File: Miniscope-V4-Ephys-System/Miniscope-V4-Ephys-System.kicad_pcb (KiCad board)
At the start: 4 copper layers, 24.2 x 15.5 mm, 67 parts, among them J1 34 Circuit Slimslack Connector, J10 Conn_01x01, J11 Conn_01x01, J12 Conn_01x01, J13 Conn_01x01, J14 Conn_01x05, J15 Conn_01x01, J16 Conn_01x01, J17 Conn_01x01, J18 Conn_01x01, J19 Conn_01x01, J2 Conn_01x01, J20 Conn_01x01, J21 Conn_01x01, J22 Conn_01x01, J23 Conn_01x01, J24 Conn_01x01, J25 Conn_01x01, J26 Conn_01x01, J27 Conn_01x01, J28 Conn_01x01, J3 Conn_01x01, J4 Conn_01x01, J5 Conn_01x01, J6 Conn_01x01, J7 Conn_01x01, J8 Conn_01x01, J9 Conn_01x01, Q1 MMBT3904LP-7B, U1 RHD2132, U2 TXB0304RUT, U3 MCP1711T-30I/5X, U4 ATSAME70N21A-CN, U5 MCP1711T-18I/5X, Y1 SMD_CRYSTAL

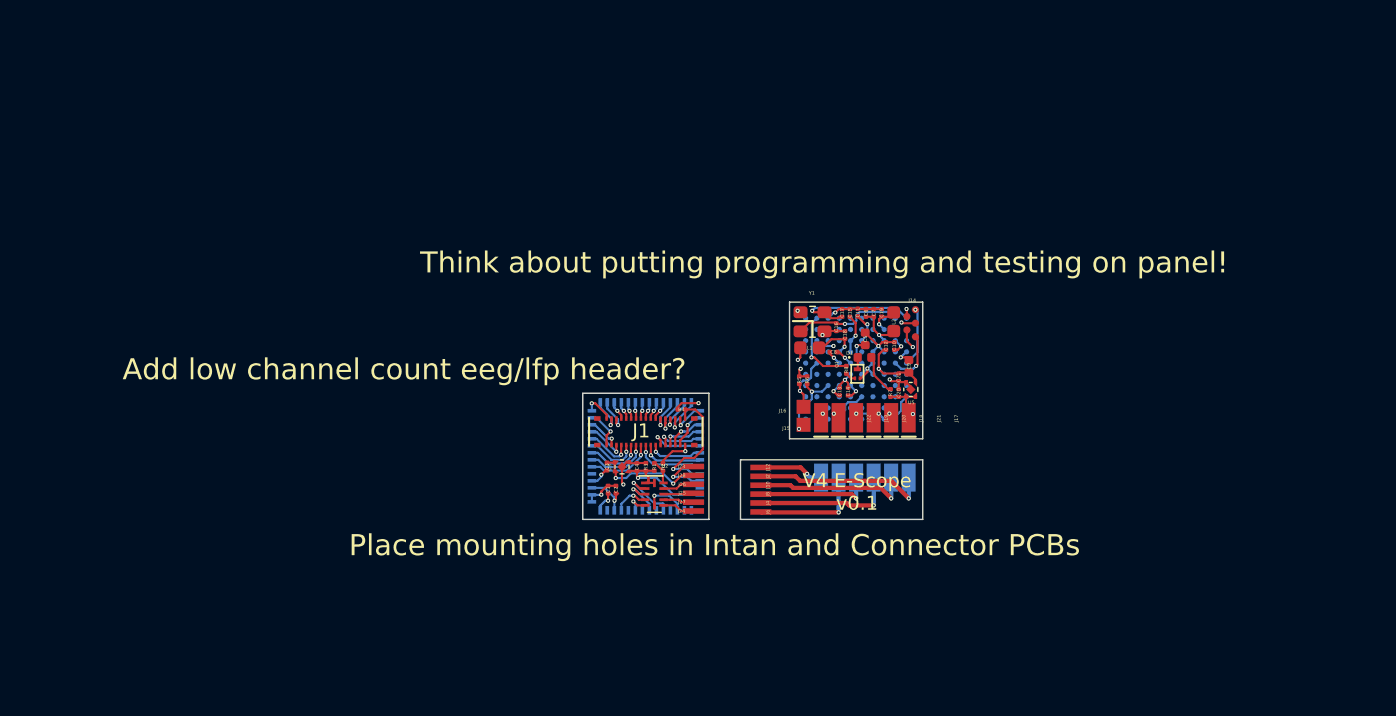
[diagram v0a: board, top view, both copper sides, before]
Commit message: Add mouse bites and panel the 3 PCBs.
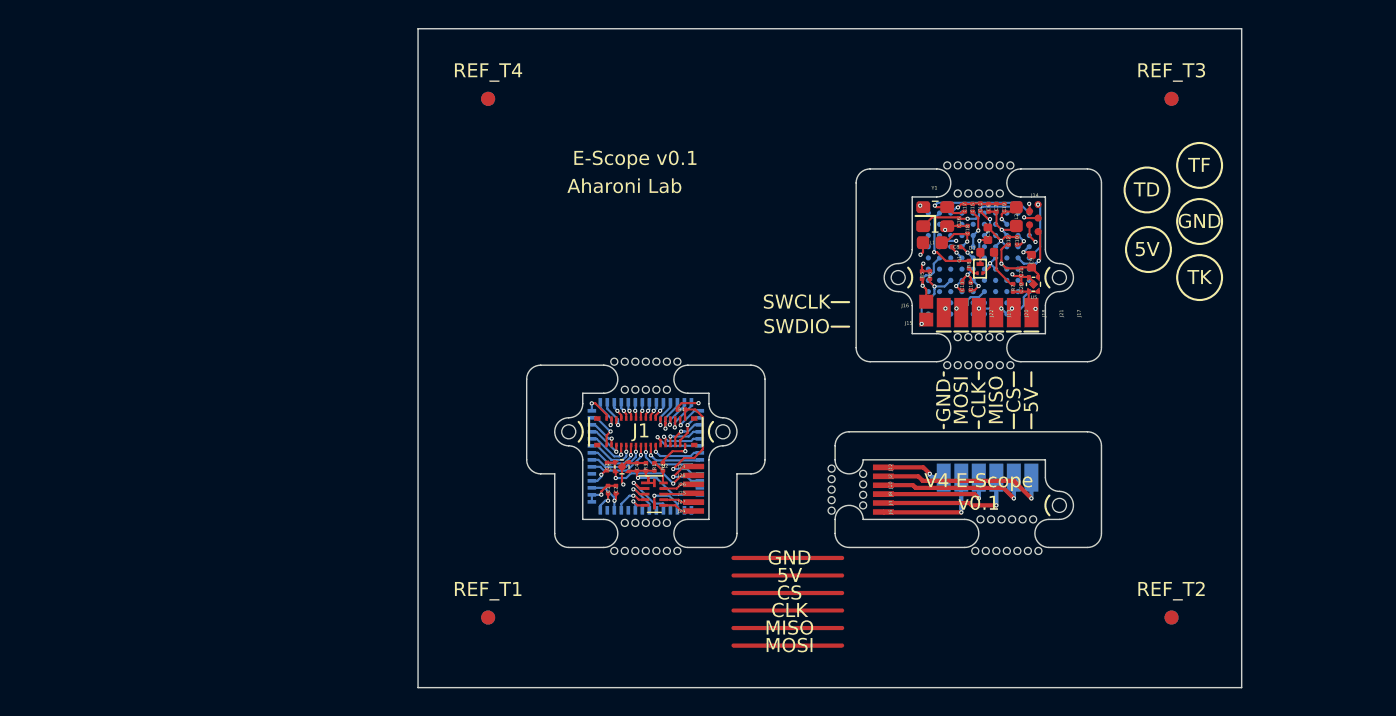
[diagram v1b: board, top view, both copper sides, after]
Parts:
- added HOLE: Conn_1x1_700_Circular_Pad, .Connector:Conn_1x1_700_Circular_Pad, F.Cu at (138.9, 135.0)
- added HOLE: Conn_1x1_700_Circular_Pad, .Connector:Conn_1x1_700_Circular_Pad, F.Cu at (137.0, 137.2)
- added HOLE: Conn_1x1_700_Circular_Pad, .Connector:Conn_1x1_700_Circular_Pad, F.Cu at (136.6, 135.0)
- added HOLE: Conn_1x1_700_Circular_Pad, .Connector:Conn_1x1_700_Circular_Pad, F.Cu at (135.9, 135.0)
- added HOLE: Conn_1x1_700_Circular_Pad, .Connector:Conn_1x1_700_Circular_Pad, F.Cu at (135.5, 137.2)
- added HOLE: Conn_1x1_700_Circular_Pad, .Connector:Conn_1x1_700_Circular_Pad, F.Cu at (124.5, 131.4)
- added HOLE: Conn_1x1_700_Circular_Pad, .Connector:Conn_1x1_700_Circular_Pad, F.Cu at (124.5, 134.4)
- added HOLE: Conn_1x1_700_Circular_Pad, .Connector:Conn_1x1_700_Circular_Pad, F.Cu at (126.8, 131.8)
- added HOLE: Conn_1x1_700_Circular_Pad, .Connector:Conn_1x1_700_Circular_Pad, F.Cu at (113.5, 137.2)
- added HOLE: Conn_1x1_700_Circular_Pad, .Connector:Conn_1x1_700_Circular_Pad, F.Cu at (109.0, 137.2)
- added HOLE: Conn_1x1_700_Circular_Pad, .Connector:Conn_1x1_700_Circular_Pad, F.Cu at (109.0, 123.8)
- added HOLE: Conn_1x1_700_Circular_Pad, .Connector:Conn_1x1_700_Circular_Pad, F.Cu at (139.2, 137.2)
- added HOLE: Conn_1x1_700_Circular_Pad, .Connector:Conn_1x1_700_Circular_Pad, F.Cu at (113.5, 123.8)
- added HOLE: Conn_1x1_700_Circular_Pad, .Connector:Conn_1x1_700_Circular_Pad, F.Cu at (132.8, 109.8)
- added HOLE: Conn_1x1_700_Circular_Pad, .Connector:Conn_1x1_700_Circular_Pad, F.Cu at (137.2, 109.8)
- added HOLE: Conn_1x1_700_Circular_Pad, .Connector:Conn_1x1_700_Circular_Pad, F.Cu at (137.2, 124.0)
- added HOLE: Conn_1x1_700_Circular_Pad, .Connector:Conn_1x1_700_Circular_Pad, F.Cu at (132.8, 124.0)
- added HOLE: Conn_1x1_700_Circular_Pad, .Connector:Conn_1x1_700_Circular_Pad, F.Cu at (124.5, 132.9)
- added HOLE: Conn_1x1_700_Circular_Pad, .Connector:Conn_1x1_700_Circular_Pad, F.Cu at (126.8, 132.5)
- added HOLE: Conn_1x1_700_Circular_Pad, .Connector:Conn_1x1_700_Circular_Pad, F.Cu at (124.5, 133.6)
- added HOLE: Conn_1x1_700_Circular_Pad, .Connector:Conn_1x1_700_Circular_Pad, F.Cu at (126.8, 134.0)
- added HOLE: Conn_1x1_700_Circular_Pad, .Connector:Conn_1x1_700_Circular_Pad, F.Cu at (126.8, 133.2)
- added HOLE: Conn_1x1_700_Circular_Pad, .Connector:Conn_1x1_700_Circular_Pad, F.Cu at (134.8, 137.2)
- added HOLE: Conn_1x1_700_Circular_Pad, .Connector:Conn_1x1_700_Circular_Pad, F.Cu at (124.5, 132.1)
- added HOLE: Conn_1x1_700_Circular_Pad, .Connector:Conn_1x1_700_Circular_Pad, F.Cu at (135.8, 122.0)
- added HOLE: Conn_1x1_700_Circular_Pad, .Connector:Conn_1x1_700_Circular_Pad, F.Cu at (134.2, 124.0)
- added HOLE: Conn_1x1_700_Circular_Pad, .Connector:Conn_1x1_700_Circular_Pad, F.Cu at (133.5, 122.0)
- added HOLE: Conn_1x1_700_Circular_Pad, .Connector:Conn_1x1_700_Circular_Pad, F.Cu at (136.5, 122.0)
- added HOLE: Conn_1x1_700_Circular_Pad, .Connector:Conn_1x1_700_Circular_Pad, F.Cu at (135.8, 124.0)
- added HOLE: Conn_1x1_700_Circular_Pad, .Connector:Conn_1x1_700_Circular_Pad, F.Cu at (136.5, 124.0)
- added HOLE: Conn_1x1_700_Circular_Pad, .Connector:Conn_1x1_700_Circular_Pad, F.Cu at (135.0, 124.0)
- added HOLE: Conn_1x1_700_Circular_Pad, .Connector:Conn_1x1_700_Circular_Pad, F.Cu at (135.0, 122.0)
- added HOLE: Conn_1x1_700_Circular_Pad, .Connector:Conn_1x1_700_Circular_Pad, F.Cu at (134.2, 122.0)
- added HOLE: Conn_1x1_700_Circular_Pad, .Connector:Conn_1x1_700_Circular_Pad, F.Cu at (137.4, 135.0)
- added HOLE: Conn_1x1_700_Circular_Pad, .Connector:Conn_1x1_700_Circular_Pad, F.Cu at (133.5, 124.0)
- added HOLE: Conn_1x1_700_Circular_Pad, .Connector:Conn_1x1_700_Circular_Pad, F.Cu at (134.2, 111.8)
- added HOLE: Conn_1x1_700_Circular_Pad, .Connector:Conn_1x1_700_Circular_Pad, F.Cu at (135.8, 109.8)
- added HOLE: Conn_1x1_700_Circular_Pad, .Connector:Conn_1x1_700_Circular_Pad, F.Cu at (136.5, 111.8)
- added HOLE: Conn_1x1_700_Circular_Pad, .Connector:Conn_1x1_700_Circular_Pad, F.Cu at (133.5, 111.8)
- added HOLE: Conn_1x1_700_Circular_Pad, .Connector:Conn_1x1_700_Circular_Pad, F.Cu at (134.2, 109.8)
- added HOLE: Conn_1x1_700_Circular_Pad, .Connector:Conn_1x1_700_Circular_Pad, F.Cu at (133.5, 109.8)
- added HOLE: Conn_1x1_700_Circular_Pad, .Connector:Conn_1x1_700_Circular_Pad, F.Cu at (135.0, 109.8)
- added HOLE: Conn_1x1_700_Circular_Pad, .Connector:Conn_1x1_700_Circular_Pad, F.Cu at (135.0, 111.8)
- added HOLE: Conn_1x1_700_Circular_Pad, .Connector:Conn_1x1_700_Circular_Pad, F.Cu at (135.8, 111.8)
- added HOLE: Conn_1x1_700_Circular_Pad, .Connector:Conn_1x1_700_Circular_Pad, F.Cu at (136.2, 137.2)
- added HOLE: Conn_1x1_700_Circular_Pad, .Connector:Conn_1x1_700_Circular_Pad, F.Cu at (136.5, 109.8)
- added HOLE: Conn_1x1_700_Circular_Pad, .Connector:Conn_1x1_700_Circular_Pad, F.Cu at (110.5, 123.8)
- added HOLE: Conn_1x1_700_Circular_Pad, .Connector:Conn_1x1_700_Circular_Pad, F.Cu at (109.8, 123.8)
- added HOLE: Conn_1x1_700_Circular_Pad, .Connector:Conn_1x1_700_Circular_Pad, F.Cu at (112.0, 123.8)
- added HOLE: Conn_1x1_700_Circular_Pad, .Connector:Conn_1x1_700_Circular_Pad, F.Cu at (112.8, 123.8)
- added HOLE: Conn_1x1_700_Circular_Pad, .Connector:Conn_1x1_700_Circular_Pad, F.Cu at (111.2, 123.8)
- added HOLE: Conn_1x1_700_Circular_Pad, .Connector:Conn_1x1_700_Circular_Pad, F.Cu at (110.5, 125.8)
- added HOLE: Conn_1x1_700_Circular_Pad, .Connector:Conn_1x1_700_Circular_Pad, F.Cu at (109.8, 125.8)
- added HOLE: Conn_1x1_700_Circular_Pad, .Connector:Conn_1x1_700_Circular_Pad, F.Cu at (112.0, 125.8)
- added HOLE: Conn_1x1_700_Circular_Pad, .Connector:Conn_1x1_700_Circular_Pad, F.Cu at (112.8, 125.8)
- added HOLE: Conn_1x1_700_Circular_Pad, .Connector:Conn_1x1_700_Circular_Pad, F.Cu at (135.1, 135.0)
- added HOLE: Conn_1x1_700_Circular_Pad, .Connector:Conn_1x1_700_Circular_Pad, F.Cu at (111.2, 125.8)
- added HOLE: Conn_1x1_700_Circular_Pad, .Connector:Conn_1x1_700_Circular_Pad, F.Cu at (110.5, 137.2)
- added HOLE: Conn_1x1_700_Circular_Pad, .Connector:Conn_1x1_700_Circular_Pad, F.Cu at (109.8, 137.2)
- added HOLE: Conn_1x1_700_Circular_Pad, .Connector:Conn_1x1_700_Circular_Pad, F.Cu at (112.0, 137.2)
- added HOLE: Conn_1x1_700_Circular_Pad, .Connector:Conn_1x1_700_Circular_Pad, F.Cu at (112.8, 137.2)
- added HOLE: Conn_1x1_700_Circular_Pad, .Connector:Conn_1x1_700_Circular_Pad, F.Cu at (111.2, 137.2)
- added HOLE: Conn_1x1_700_Circular_Pad, .Connector:Conn_1x1_700_Circular_Pad, F.Cu at (112.8, 135.2)
- added HOLE: Conn_1x1_700_Circular_Pad, .Connector:Conn_1x1_700_Circular_Pad, F.Cu at (112.0, 135.2)
- added HOLE: Conn_1x1_700_Circular_Pad, .Connector:Conn_1x1_700_Circular_Pad, F.Cu at (111.2, 135.2)
- added HOLE: Conn_1x1_700_Circular_Pad, .Connector:Conn_1x1_700_Circular_Pad, F.Cu at (110.5, 135.2)
- added HOLE: Conn_1x1_700_Circular_Pad, .Connector:Conn_1x1_700_Circular_Pad, F.Cu at (138.1, 135.0)
- added HOLE: Conn_1x1_700_Circular_Pad, .Connector:Conn_1x1_700_Circular_Pad, F.Cu at (109.8, 135.2)
- added HOLE: Conn_1x1_700_Circular_Pad, .Connector:Conn_1x1_700_Circular_Pad, F.Cu at (140.8, 134.0)
- added HOLE: Conn_1x1_700_Circular_Pad, .Connector:Conn_1x1_700_Circular_Pad, F.Cu at (105.8, 128.8)
- added HOLE: Conn_1x1_700_Circular_Pad, .Connector:Conn_1x1_700_Circular_Pad, F.Cu at (116.8, 128.8)
- added HOLE: Conn_1x1_700_Circular_Pad, .Connector:Conn_1x1_700_Circular_Pad, F.Cu at (140.8, 117.8)
- added HOLE: Conn_1x1_700_Circular_Pad, .Connector:Conn_1x1_700_Circular_Pad, F.Cu at (129.2, 117.8)
- added HOLE: Conn_1x1_700_Circular_Pad, .Connector:Conn_1x1_700_Circular_Pad, F.Cu at (137.8, 137.2)
- added HOLE: Conn_1x1_700_Circular_Pad, .Connector:Conn_1x1_700_Circular_Pad, F.Cu at (138.5, 137.2)
- added REF_B1: Fiducial_1mm_Mask2mm, Fiducial:Fiducial_1mm_Mask2mm, B.Cu at (100.0, 142.0)
- added REF_B2: Fiducial_1mm_Mask2mm, Fiducial:Fiducial_1mm_Mask2mm, B.Cu at (148.8, 142.0)
- added REF_B3: Fiducial_1mm_Mask2mm, Fiducial:Fiducial_1mm_Mask2mm, B.Cu at (148.8, 105.0)
- added REF_B4: Fiducial_1mm_Mask2mm, Fiducial:Fiducial_1mm_Mask2mm, B.Cu at (100.0, 105.0)
- added REF_T1: Fiducial_1mm_Mask2mm, Fiducial:Fiducial_1mm_Mask2mm, F.Cu at (100.0, 142.0)
- added REF_T2: Fiducial_1mm_Mask2mm, Fiducial:Fiducial_1mm_Mask2mm, F.Cu at (148.8, 142.0)
- added REF_T3: Fiducial_1mm_Mask2mm, Fiducial:Fiducial_1mm_Mask2mm, F.Cu at (148.8, 105.0)
- added REF_T4: Fiducial_1mm_Mask2mm, Fiducial:Fiducial_1mm_Mask2mm, F.Cu at (100.0, 105.0)
- moved C11 11.5 mm to (135.1, 112.7)
- moved C13 11.5 mm to (133.8, 118.4)
- moved C14 11.5 mm to (134.4, 118.4)
- moved C16 11.5 mm to (133.6, 113.8)
- moved C18 11.5 mm to (134.2, 114.3)
- moved C5 11.5 mm to (135.6, 114.6)
- moved C7 11.5 mm to (136.3, 112.8)
- moved C10 11.5 mm to (137.7, 115.1)
- moved C12 11.5 mm to (137.1, 115.1)
- moved C17 11.5 mm to (134.0, 112.8)
- moved C19 11.5 mm to (136.8, 112.8)
- moved C20 11.5 mm to (138.0, 118.5)
- moved C21 11.5 mm to (138.0, 117.4)
- moved C8 11.5 mm to (133.4, 115.6)
- moved C9 11.5 mm to (138.8, 116.6)
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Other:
- board size 24.2 x 15.5 mm -> 58.8 x 47 mm
- board text added: "5V"
- board text added: "Aharoni Lab"
- board text added: "CLK"
- board text added: "CS"
- board text added: "E-Scope v0.1"
- board text added: "GND"
- board text added: "MISO"
- board text added: "MOSI"
- board text added: "SWCLK"
- board text added: "SWDIO"
- board text added: "TD"
- board text added: "TF"
- board text added: "TK"
- board text removed: "Add low channel count eeg/lfp header?"
- board text removed: "Place mounting holes in Intan and Connector PCBs"
- board text removed: "Think about putting programming and testing on panel!"

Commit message: Add files via upload
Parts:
- added HOLE: Conn_1x1_700_Circular_Pad, .Connector:Conn_1x1_700_Circular_Pad, F.Cu at (107.8, 119.9)
- added HOLE: Conn_1x1_700_Circular_Pad, .Connector:Conn_1x1_700_Circular_Pad, F.Cu at (110.8, 111.0)
- added HOLE: Conn_1x1_700_Circular_Pad, .Connector:Conn_1x1_700_Circular_Pad, F.Cu at (110.0, 113.0)
- added HOLE: Conn_1x1_700_Circular_Pad, .Connector:Conn_1x1_700_Circular_Pad, F.Cu at (109.3, 113.0)
- added HOLE: Conn_1x1_700_Circular_Pad, .Connector:Conn_1x1_700_Circular_Pad, F.Cu at (109.3, 111.0)
- added HOLE: Conn_1x1_700_Circular_Pad, .Connector:Conn_1x1_700_Circular_Pad, F.Cu at (107.8, 111.0)
- added HOLE: Conn_1x1_700_Circular_Pad, .Connector:Conn_1x1_700_Circular_Pad, F.Cu at (108.5, 111.0)
- added HOLE: Conn_1x1_700_Circular_Pad, .Connector:Conn_1x1_700_Circular_Pad, F.Cu at (107.8, 113.0)
- added HOLE: Conn_1x1_700_Circular_Pad, .Connector:Conn_1x1_700_Circular_Pad, F.Cu at (110.8, 113.0)
- added HOLE: Conn_1x1_700_Circular_Pad, .Connector:Conn_1x1_700_Circular_Pad, F.Cu at (110.0, 111.0)
- added HOLE: Conn_1x1_700_Circular_Pad, .Connector:Conn_1x1_700_Circular_Pad, F.Cu at (108.5, 113.0)
- added HOLE: Conn_1x1_700_Circular_Pad, .Connector:Conn_1x1_700_Circular_Pad, F.Cu at (108.5, 121.9)
- added HOLE: Conn_1x1_700_Circular_Pad, .Connector:Conn_1x1_700_Circular_Pad, F.Cu at (107.8, 121.9)
- added HOLE: Conn_1x1_700_Circular_Pad, .Connector:Conn_1x1_700_Circular_Pad, F.Cu at (108.5, 119.9)
- added HOLE: Conn_1x1_700_Circular_Pad, .Connector:Conn_1x1_700_Circular_Pad, F.Cu at (109.3, 119.9)
- added HOLE: Conn_1x1_700_Circular_Pad, .Connector:Conn_1x1_700_Circular_Pad, F.Cu at (109.3, 121.9)
- added HOLE: Conn_1x1_700_Circular_Pad, .Connector:Conn_1x1_700_Circular_Pad, F.Cu at (110.8, 121.9)
- added HOLE: Conn_1x1_700_Circular_Pad, .Connector:Conn_1x1_700_Circular_Pad, F.Cu at (110.0, 121.9)
- added HOLE: Conn_1x1_700_Circular_Pad, .Connector:Conn_1x1_700_Circular_Pad, F.Cu at (110.8, 119.9)
- added HOLE: Conn_1x1_700_Circular_Pad, .Connector:Conn_1x1_700_Circular_Pad, F.Cu at (110.0, 119.9)
- added HOLE: Conn_1x1_700_Circular_Pad, .Connector:Conn_1x1_700_Circular_Pad, F.Cu at (107.0, 121.9)
- added HOLE: Conn_1x1_700_Circular_Pad, .Connector:Conn_1x1_700_Circular_Pad, F.Cu at (111.5, 121.9)
- added HOLE: Conn_1x1_700_Circular_Pad, .Connector:Conn_1x1_700_Circular_Pad, F.Cu at (111.5, 111.0)
- added HOLE: Conn_1x1_700_Circular_Pad, .Connector:Conn_1x1_700_Circular_Pad, F.Cu at (107.0, 111.0)
- added HOLE: Conn_1x1_700_Circular_Pad, .Connector:Conn_1x1_700_Circular_Pad, F.Cu at (103.5, 115.6)
- added HOLE: Conn_1x1_700_Circular_Pad, .Connector:Conn_1x1_700_Circular_Pad, F.Cu at (115.0, 115.6)
- added J10: Conn_01x01, .Connector:Conn_1x1_250x750_Pad, F.Cu at (105.7, 117.2)
- added J12: Conn_01x01, .Connector:Conn_1x1_250x750_Pad, F.Cu at (105.7, 115.9)
- added J13: Conn_01x01, .Connector:Conn_1x1_250x750_Pad, B.Cu at (113.3, 118.4)
- added J2: Conn_01x01, .Connector:Conn_1x1_250x750_Pad, F.Cu at (105.7, 116.6)
- added J3: Conn_01x01, .Connector:Conn_1x1_250x750_Pad, B.Cu at (105.4, 118.9)
- added J3: Conn_01x01, .Connector:Conn_1x1_250x750_Pad, B.Cu at (105.4, 117.6)
- added J3: Conn_01x01, .Connector:Conn_1x1_250x750_Pad, B.Cu at (107.1, 118.4)
- added J4: Conn_01x01, .Connector:Conn_1x1_250x750_Pad, F.Cu at (105.7, 118.5)
- added J6: Conn_01x01, .Connector:Conn_1x1_250x750_Pad, F.Cu at (105.7, 119.1)
- added J8: Conn_01x01, .Connector:Conn_1x1_250x750_Pad, F.Cu at (105.7, 117.8)
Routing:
- net (no net): track 0.00 -> 28.6 mm, vias 0 -> 2
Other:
- outline, holes or cut-outs redrawn

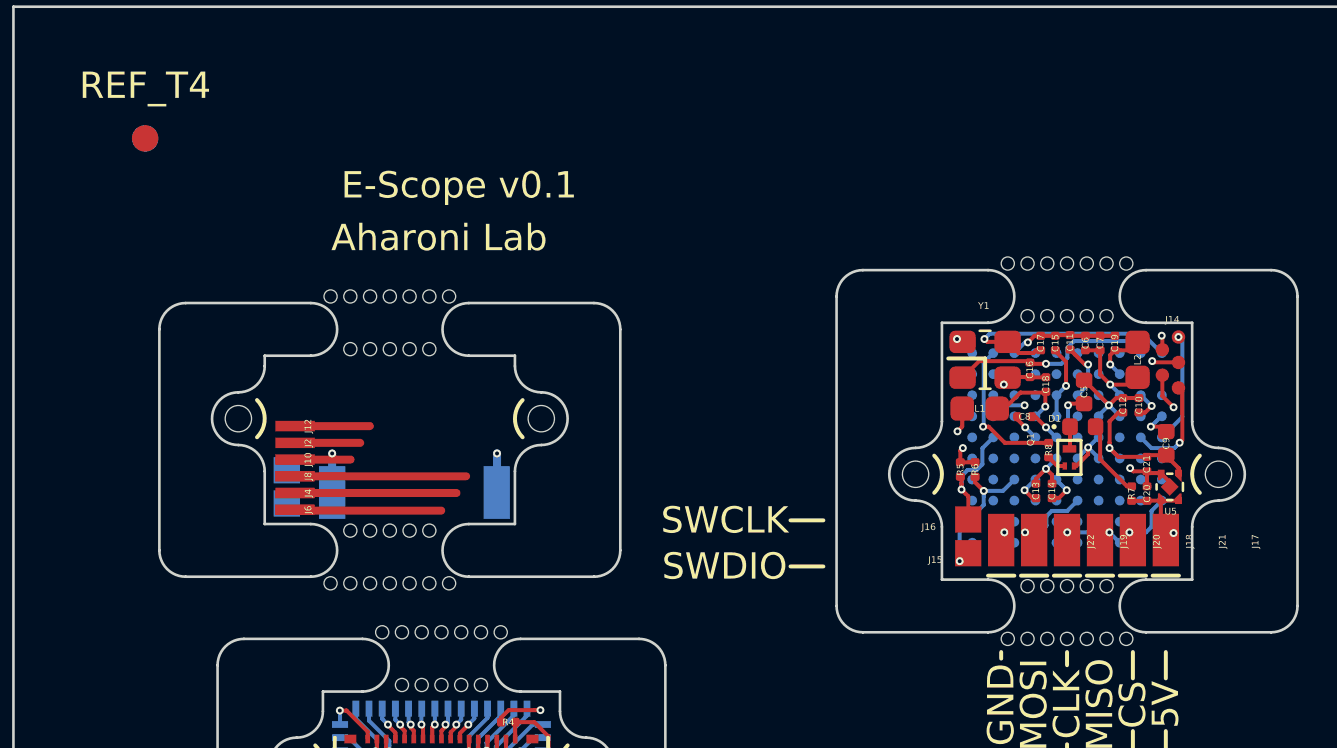
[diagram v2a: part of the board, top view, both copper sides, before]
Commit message: Revert "updated ephys pcb with low profile connectors and started programming board"
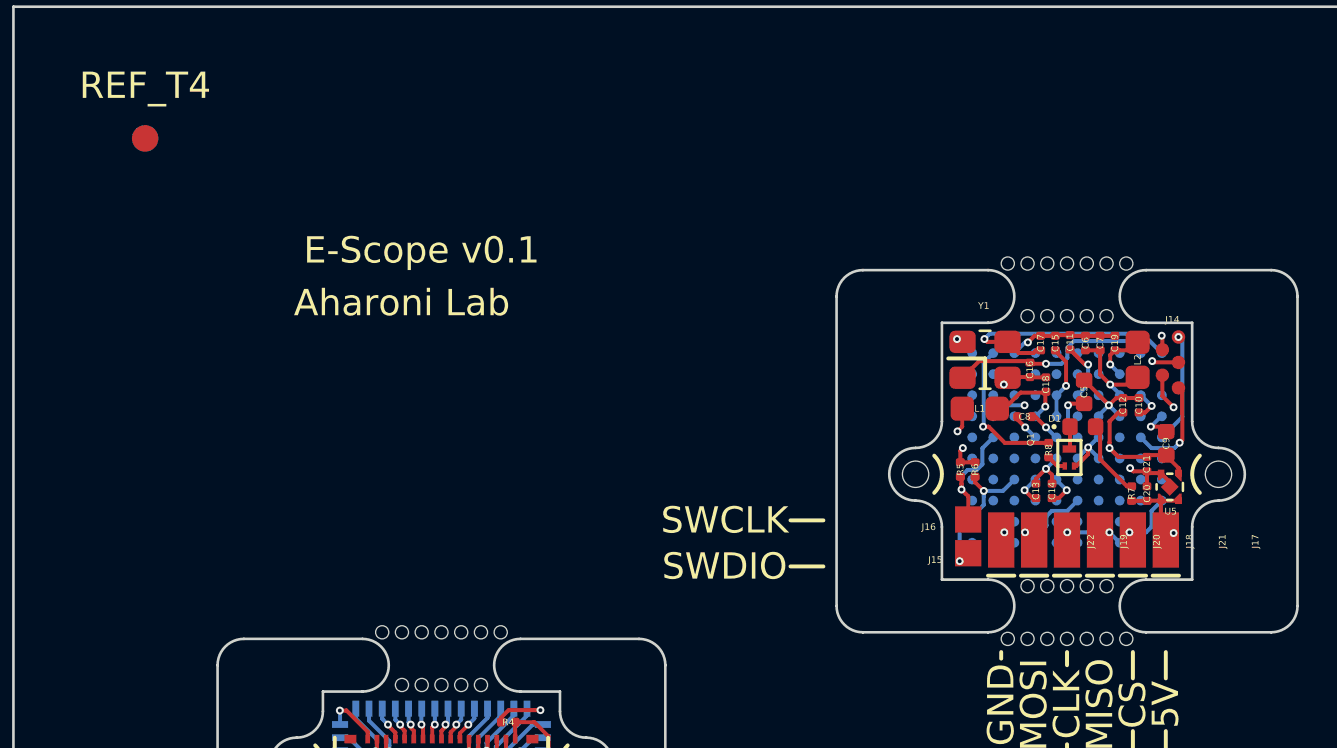
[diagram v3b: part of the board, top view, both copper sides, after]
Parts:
- removed the HOLE at (107.8, 119.9)
- removed the HOLE at (110.8, 111.0)
- removed the HOLE at (110.0, 113.0)
- removed the HOLE at (109.3, 113.0)
- removed the HOLE at (109.3, 111.0)
- removed the HOLE at (107.8, 111.0)
- removed the HOLE at (108.5, 111.0)
- removed the HOLE at (107.8, 113.0)
- removed the HOLE at (110.8, 113.0)
- removed the HOLE at (110.0, 111.0)
- removed the HOLE at (108.5, 113.0)
- removed the HOLE at (108.5, 121.9)
- removed the HOLE at (107.8, 121.9)
- removed the HOLE at (108.5, 119.9)
- removed the HOLE at (109.3, 119.9)
- removed the HOLE at (109.3, 121.9)
- removed the HOLE at (110.8, 121.9)
- removed the HOLE at (110.0, 121.9)
- removed the HOLE at (110.8, 119.9)
- removed the HOLE at (110.0, 119.9)
- removed the HOLE at (107.0, 121.9)
- removed the HOLE at (111.5, 121.9)
- removed the HOLE at (111.5, 111.0)
- removed the HOLE at (107.0, 111.0)
- removed the HOLE at (103.5, 115.6)
- removed the HOLE at (115.0, 115.6)
- removed the J10 at (105.7, 117.2)
- removed the J12 at (105.7, 115.9)
- removed the J13 at (113.3, 118.4)
- removed the J2 at (105.7, 116.6)
- removed the J3 at (105.4, 118.9)
- removed the J3 at (105.4, 117.6)
- removed the J3 at (107.1, 118.4)
- removed the J4 at (105.7, 118.5)
- removed the J6 at (105.7, 119.1)
- removed the J8 at (105.7, 117.8)
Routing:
- net (no net): track 28.6 -> 0.00 mm, vias 2 -> 0
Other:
- outline, holes or cut-outs redrawn

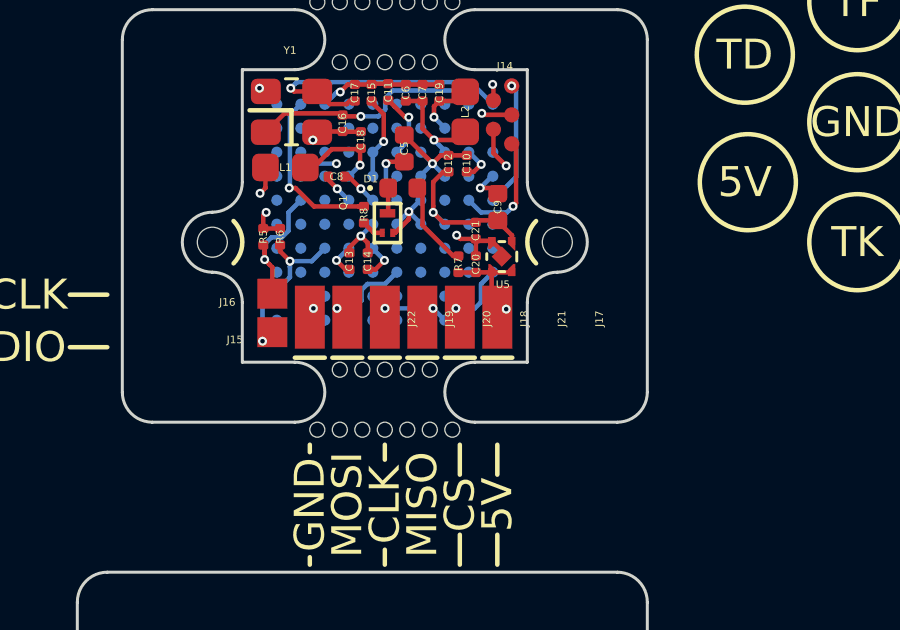
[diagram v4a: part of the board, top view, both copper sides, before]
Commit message: Switch spring connectors to a lower profile option
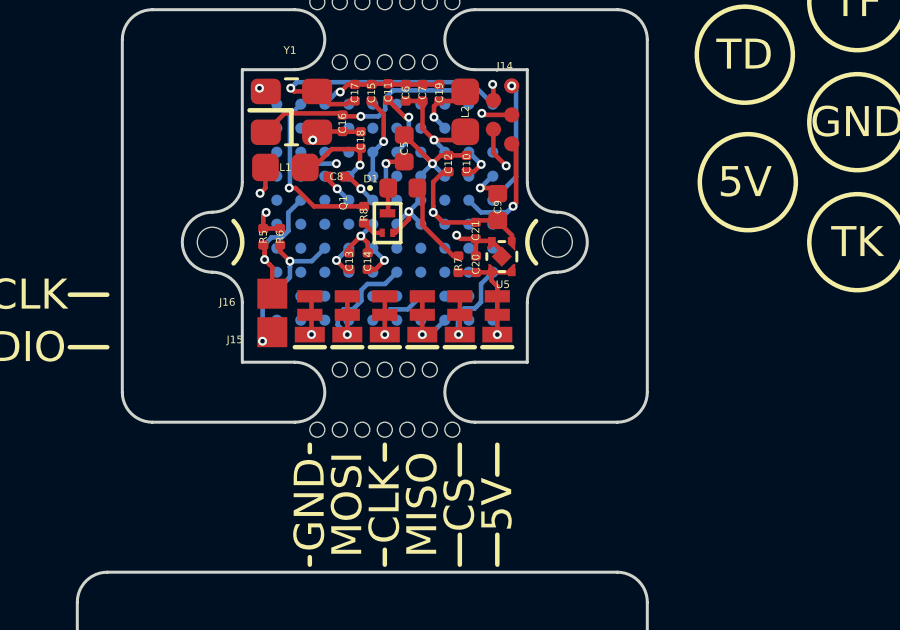
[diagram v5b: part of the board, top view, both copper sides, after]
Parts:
- J17, J18, J19, J20, J21, J22: footprint .Connector:Spring_2306654_3 -> .Connector:Spring_2306334
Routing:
- net /MCU/SPI0_MOSI: track 2.70 -> 4.83 mm
- net /MCU/SPI0_SPCK: track 1.36 -> 3.39 mm
- net /MCU/SPI0_NPCS0: track 2.08 -> 4.04 mm
- net +5V: track 30.3 -> 32.0 mm
- net /MCU/SPI0_MISO: track 0.56 -> 2.23 mm
- net GND: track 44.6 -> 45.9 mm
